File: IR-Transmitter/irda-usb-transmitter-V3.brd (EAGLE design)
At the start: 50 x 50 mm, 20 parts, among them IC1 FT232RL, IC2 MCP2120, Q2 7.3728MHz

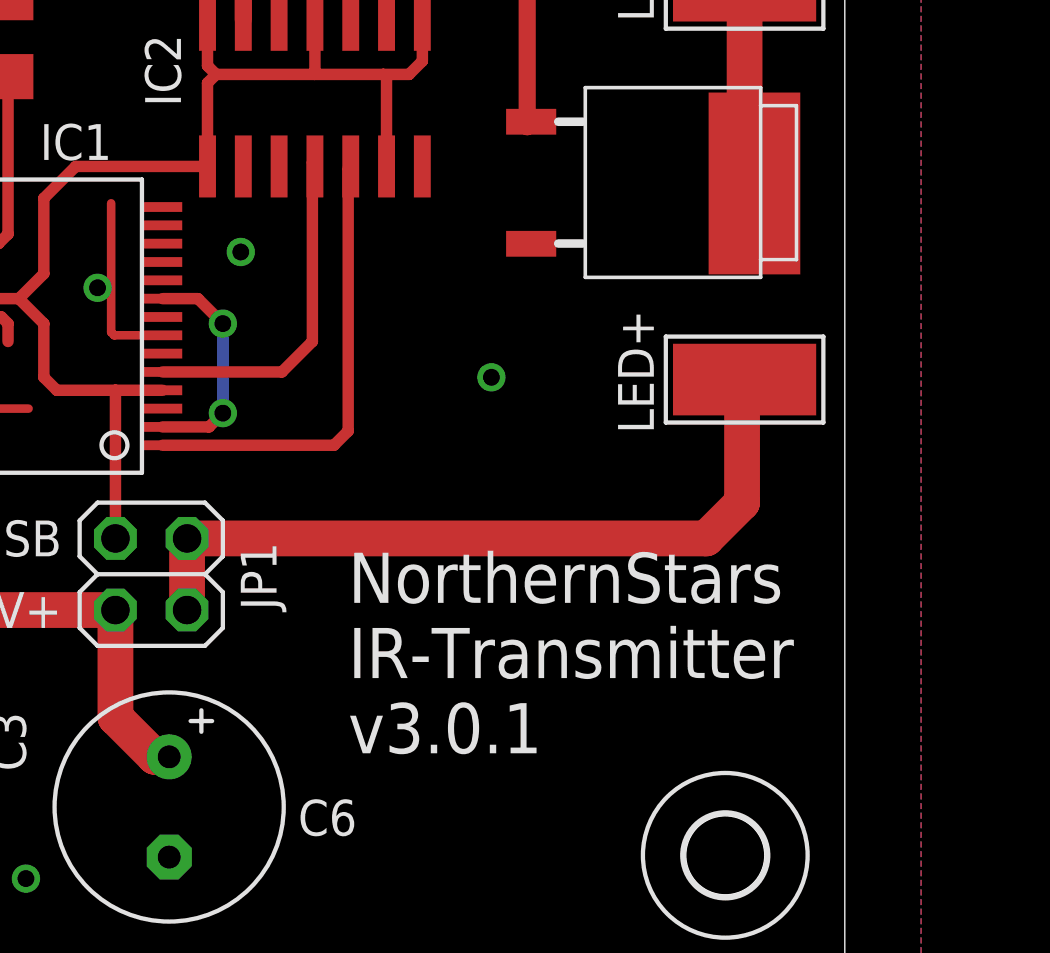
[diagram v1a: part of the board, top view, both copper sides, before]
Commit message: Added optional resistors R2  & R3 to schematics and layout.
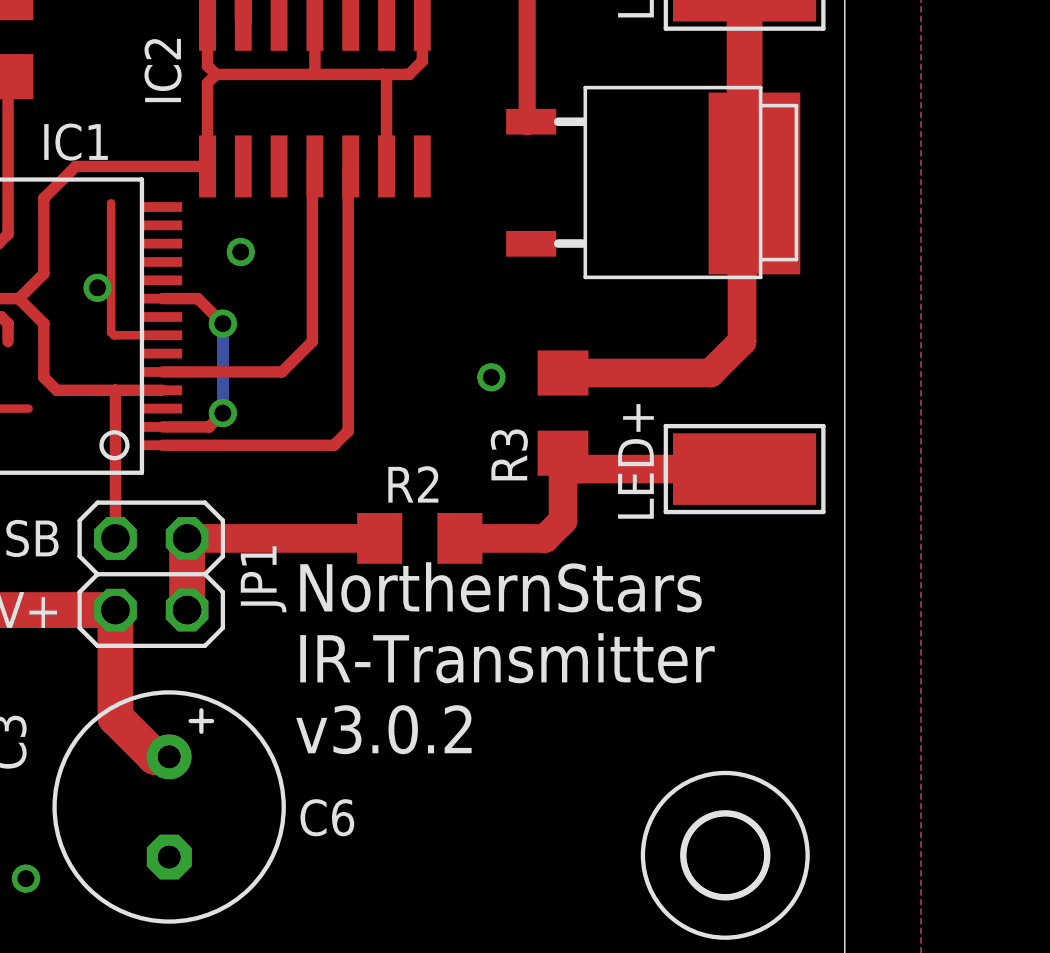
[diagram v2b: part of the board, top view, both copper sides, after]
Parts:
- added R2, R3: (no value), rcl:R1206
- moved LED+ 3.18 mm to (46.4, 17.7)
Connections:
- new net N$1: LED+.1, R2.1, R3.2
- net IRLEDS-: now also R3.1
- net VCC: now also R2.2; no longer LED+.1
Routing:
- net VCC: track 27.2 -> 9.37 mm
- net N$1: track 0.00 -> 13.0 mm
- net IRLEDS-: track 7.16 -> 19.8 mm
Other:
- board text added: "NorthernStars IR-Transmitter v3.0.2"
- board text removed: "NorthernStars IR-Transmitter v3.0.1"
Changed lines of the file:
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@@
 <wire x1="7.65" y1="36" x2="7.65" y2="50" width="0" layer="20"/>
 <rectangle x1="8.255" y1="10.795" x2="15.24" y2="14.605" layer="1"/>
-<text x="32.385" y="7.62" size="1.778" layer="25">NorthernStars
+<text x="30.48" y="7.62" size="1.6764" layer="25" font="vector">NorthernStars
 IR-Transmitter
-v3.0.1</text>
+v3.0.2</text>
 <text x="22.225" y="15.875" size="1.27" layer="25" rot="R180">V_USB</text>
 <text x="22.225" y="13.335" size="1.27" layer="25" rot="R180">V+</text>
@@
 <attribute name="VALUE" x="27.385" y="30.443" size="1.27" layer="27"/>
 </element>
-<element name="LED+" library="wirepad" package="5-2,5" value="IR-LED" x="46.445" y="20.875" smashed="yes" rot="R90">
-<attribute name="NAME" x="43.227" y="18.96" size="1.27" layer="25" ratio="10" rot="R90"/>
-<attribute name="VALUE" x="43.645" y="20.775" size="0.0254" layer="27" rot="R90"/>
+<element name="LED+" library="wirepad" package="5-2,5" value="IR-LED" x="46.445" y="17.7" smashed="yes" rot="R90">
+<attribute name="NAME" x="43.227" y="15.785" size="1.27" layer="25" ratio="10" rot="R90"/>
+<attribute name="VALUE" x="43.645" y="17.6" size="0.0254" layer="27" rot="R90"/>
 </element>
 <element name="LED-" library="wirepad" package="5-2,5" value="IR-LED" x="46.445" y="34.845" smashed="yes" rot="R90">
@@
 <attribute name="NAME" x="29.845" y="12.7" size="1.27" layer="25" ratio="10" rot="R90"/>
 <attribute name="VALUE" x="20.955" y="16.51" size="1.27" layer="27" rot="R270"/>
+</element>
+<element name="R2" library="rcl" package="R1206" value="" x="34.925" y="15.24" smashed="yes" rot="R180">
+<attribute name="NAME" x="33.655" y="16.51" size="1.27" layer="25"/>
+<attribute name="VALUE" x="36.195" y="17.78" size="1.27" layer="27" rot="R180"/>
+</element>
+<element name="R3" library="rcl" package="R1206" value="" x="40.005" y="19.685" smashed="yes" rot="R270">
+<attribute name="NAME" x="38.735" y="17.145" size="1.27" layer="25" rot="R90"/>
+<attribute name="VALUE" x="37.465" y="20.955" size="1.27" layer="27" rot="R270"/>
 </element>
 </elements>
@@
 <wire x1="46.445" y1="34.845" x2="46.445" y2="28.18" width="1.27" layer="1"/>
 <wire x1="46.445" y1="28.18" x2="46.795" y2="27.83" width="1.27" layer="1"/>
+<contactref element="R3" pad="1"/>
+<wire x1="40.005" y1="21.107" x2="45.237" y2="21.107" width="1.016" layer="1"/>
+<wire x1="45.237" y1="21.107" x2="46.355" y2="22.225" width="1.016" layer="1"/>
+<wire x1="46.355" y1="22.225" x2="46.355" y2="27.39" width="1.016" layer="1"/>
+<wire x1="46.355" y1="27.39" x2="46.795" y2="27.83" width="1.016" layer="1"/>
 </signal>
 <signal name="+3V3">
@@
 </signal>
 <signal name="VCC">
-<contactref element="LED+" pad="1"/>
 <contactref element="JP1" pad="2"/>
 <contactref element="JP1" pad="4"/>
 <wire x1="26.67" y1="12.7" x2="26.67" y2="15.24" width="1.27" layer="1"/>
-<wire x1="26.67" y1="15.24" x2="45.085" y2="15.24" width="1.27" layer="1"/>
-<wire x1="45.085" y1="15.24" x2="46.355" y2="16.51" width="1.27" layer="1"/>
-<wire x1="46.355" y1="16.51" x2="46.355" y2="20.785" width="1.27" layer="1"/>
-<wire x1="46.355" y1="20.785" x2="46.445" y2="20.875" width="1.27" layer="1"/>
+<contactref element="R2" pad="2"/>
+<wire x1="26.67" y1="15.24" x2="33.503" y2="15.24" width="1.016" layer="1"/>
+</signal>
+<signal name="N$1">
+<contactref element="LED+" pad="1"/>
+<contactref element="R2" pad="1"/>
+<contactref element="R3" pad="2"/>
+<wire x1="36.347" y1="15.24" x2="39.37" y2="15.24" width="1.016" layer="1"/>
+<wire x1="39.37" y1="15.24" x2="40.005" y2="15.875" width="1.016" layer="1"/>
+<wire x1="40.005" y1="15.875" x2="40.005" y2="18.263" width="1.016" layer="1"/>
+<wire x1="46.445" y1="17.7" x2="40.568" y2="17.7" width="1.016" layer="1"/>
+<wire x1="40.568" y1="17.7" x2="40.005" y2="18.263" width="1.016" layer="1"/>
 </signal>
 </signals>
